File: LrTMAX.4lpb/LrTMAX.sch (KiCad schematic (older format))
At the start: 124 parts, among them J1 USB_C_Receptacle_USB2.0, J2 SM06B-SRSS-TB, Q1 2N7002, SW1 Tact_SW_8mm, SW10 EC11_SMD, SW11 EC11_SMD, SW12 EC11_SMD, SW13 EC11_SMD, SW14 EC11_SMD, SW15 EC11_SMD, SW16 EC11_SMD, SW17 EC11_SMD, SW2 Tact_SW_8mm, SW3 Tact_SW_8mm, SW4 Tact_SW_8mm, SW5 Tact_SW_8mm, SW6 Tact_SW_8mm, SW7 Tact_SW_8mm, SW8 Tact_SW_8mm, U1 STM32F072C8Tx, U3 SSD1306_OLED_0.91, U4 SPX3819M5-L3-3TR

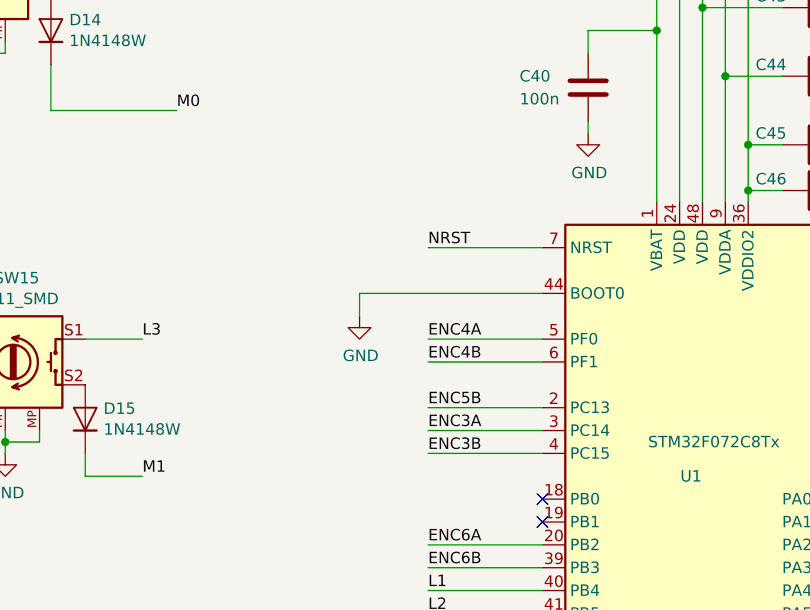
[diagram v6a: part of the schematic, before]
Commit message: 0.62-00.12cc
Modify "BOOT0" connection on PCB as "1.2cc"
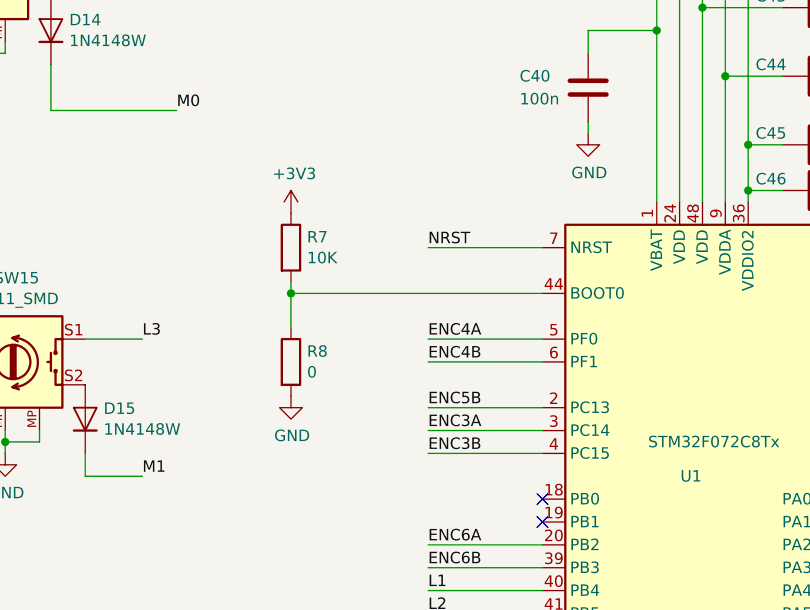
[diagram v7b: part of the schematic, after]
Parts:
- added R7: 10K, Resistor_SMD:R_0805_2012Metric, symbol Device:R
- added R8: 0, Resistor_SMD:R_0805_2012Metric, symbol Device:R
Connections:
- wire segments 509 -> 510
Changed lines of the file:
@@
 L LrE-6-rescue:GND-power #PWR0141
 U 1 1 5C4E242E
-P 7000 2950
-F 0 "#PWR0141" H 7000 2700 50  0001 C CNN
-F 1 "GND" H 7005 2777 50  0000 C CNN
-F 2 "" H 7000 2950 50  0001 C CNN
-F 3 "" H 7000 2950 50  0001 C CNN
-	1    7000 2950
-	1    0    0    -1
-$EndComp
-Wire Wire Line
-	7000 2950 7000 2850
-Wire Wire Line
-	7000 2850 7800 2850
+P 6700 3300
+F 0 "#PWR0141" H 6700 3050 50  0001 C CNN
+F 1 "GND" H 6705 3127 50  0000 C CNN
+F 2 "" H 6700 3300 50  0001 C CNN
+F 3 "" H 6700 3300 50  0001 C CNN
+	1    6700 3300
+	1    0    0    -1
+$EndComp
+Wire Wire Line
+	6700 3000 6700 2850
+Wire Wire Line
+	6700 2850 7800 2850
 Wire Wire Line
 	12500 4900 12500 4550
@@
 NoConn ~ 12300 2000
 NoConn ~ 12300 2100
+$Comp
+L Device:R R8
+U 1 1 63D44D4B
+P 6700 3150
+F 0 "R8" H 6770 3196 50  0000 L CNN
+F 1 "0" H 6770 3105 50  0000 L CNN
+F 2 "Resistor_SMD:R_0805_2012Metric" V 6630 3150 50  0001 C CNN
+F 3 "~" H 6700 3150 50  0001 C CNN
+	1    6700 3150
+	1    0    0    -1
+$EndComp
+$Comp
+L Device:R R7
+U 1 1 63DDF5C7
+P 6700 2650
+F 0 "R7" H 6770 2696 50  0000 L CNN
+F 1 "10K" H 6770 2605 50  0000 L CNN
+F 2 "Resistor_SMD:R_0805_2012Metric" V 6630 2650 50  0001 C CNN
+F 3 "~" H 6700 2650 50  0001 C CNN
+	1    6700 2650
+	1    0    0    -1
+$EndComp
+Wire Wire Line
+	6700 2800 6700 2850
+Connection ~ 6700 2850
+$Comp
+L LrE-6-rescue:+3V3-power #PWR03
+U 1 1 63E32B48
+P 6700 2500
+F 0 "#PWR03" H 6700 2350 50  0001 C CNN
+F 1 "+3V3" H 6715 2673 50  0000 C CNN
+F 2 "" H 6700 2500 50  0001 C CNN
+F 3 "" H 6700 2500 50  0001 C CNN
+	1    6700 2500
+	1    0    0    -1
+$EndComp
 $EndSCHEMATC
